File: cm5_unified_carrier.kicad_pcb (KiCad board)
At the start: 4 copper layers, 116 x 84 mm, 45 parts, among them J101 436500403, J102 484050003, J103 484050003, J104 PJ-102AH, J105 1050170001, J201 7499511002A, J401 PJ-102AH, J501 Hirose DF40C-100DS-0.4V, J601 Conn_01x02_Pin, SW501 SW_Push, U201 AG5712-LPB

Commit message: a few more minor updates
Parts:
- J201: value 7499511002A -> 7499511001A
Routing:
- net GND: vias 82 -> 81
- net /Ethernet_PoE/48V_FROM_POE: vias 29 -> 35
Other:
- board text added: "48V Input HK No PoE"
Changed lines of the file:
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@@
 			)
 		)
-		(property "Value" "7499511002A"
+		(property "Value" "7499511001A"
 			(at -5.31 23.42 0)
 			(unlocked yes)
@@
 		)
 	)
+	(gr_text "48V Input\nHK No PoE"
+		(at 120.25 62.75 0)
+		(layer "F.SilkS")
+		(effects
+			(font
+				(size 1 1)
+				(thickness 0.1)
+			)
+			(justify left bottom)
+		)
+	)
 	(gr_text "USB3 \nCamera"
 		(at 165.95 126.15 90)
@@
 	)
 	(via
-		(at 154.72 83.92)
+		(at 155.75 83.75)
 		(size 0.6)
 		(drill 0.3)
@@
 	)
 	(via
-		(at 154.58 91.07)
-		(size 0.6)
-		(drill 0.3)
-		(layers "F.Cu" "B.Cu")
-		(free yes)
-		(net 2)
-	)
-	(via
 		(at 151.26 116.64)
 		(size 0.6)
@@
 	)
 	(via
+		(at 155 87.5)
+		(size 0.6)
+		(drill 0.3)
+		(layers "F.Cu" "B.Cu")
+		(free yes)
+		(net 6)
+	)
+	(via
+		(at 154.25 84.75)
+		(size 0.6)
+		(drill 0.3)
+		(layers "F.Cu" "B.Cu")
+		(free yes)
+		(net 6)
+	)
+	(via
 		(at 156.3 96.2)
 		(size 0.6)
@@
 	)
 	(via
+		(at 153 84)
+		(size 0.6)
+		(drill 0.3)
+		(layers "F.Cu" "B.Cu")
+		(free yes)
+		(net 6)
+	)
+	(via
 		(at 137.5 92.5)
 		(size 0.6)
@@
 	)
 	(via
+		(at 154.25 86.25)
+		(size 0.6)
+		(drill 0.3)
+		(layers "F.Cu" "B.Cu")
+		(free yes)
+		(net 6)
+	)
+	(via
 		(at 154 100.2)
 		(size 0.6)
@@
 	)
 	(via
+		(at 153.25 89.75)
+		(size 0.6)
+		(drill 0.3)
+		(layers "F.Cu" "B.Cu")
+		(free yes)
+		(net 6)
+	)
+	(via
 		(at 157.2 101.5)
 		(size 0.6)
@@
 	)
 	(via
+		(at 155 89)
+		(size 0.6)
+		(drill 0.3)
+		(layers "F.Cu" "B.Cu")
+		(free yes)
+		(net 6)
+	)
+	(via
 		(at 134.7 90)
 		(size 0.6)
@@
 			)
 		)
+	)
+	(zone
+		(net 6)
+		(net_name "/Ethernet_PoE/48V_FROM_POE")
+		(layer "F.Cu")
+		(hatch edge 0.5)
+		(priority 14)
+		(connect_pads
+			(clearance 0.5)
+		)
+		(min_thickness 0.25)
+		(filled_areas_thickness no)
+		(fill yes
+			(thermal_gap 0.5)
+			(thermal_bridge_width 0.5)
+		)
+		(polygon
+			(pts
+				(xy 151.75 83.75) (xy 151.75 86.5) (xy 152.5 87.25) (xy 152.5 90.25) (xy 155.75 90.25) (xy 155.75 84.5)
+				(xy 153.75 83.75)
+			)
+		)

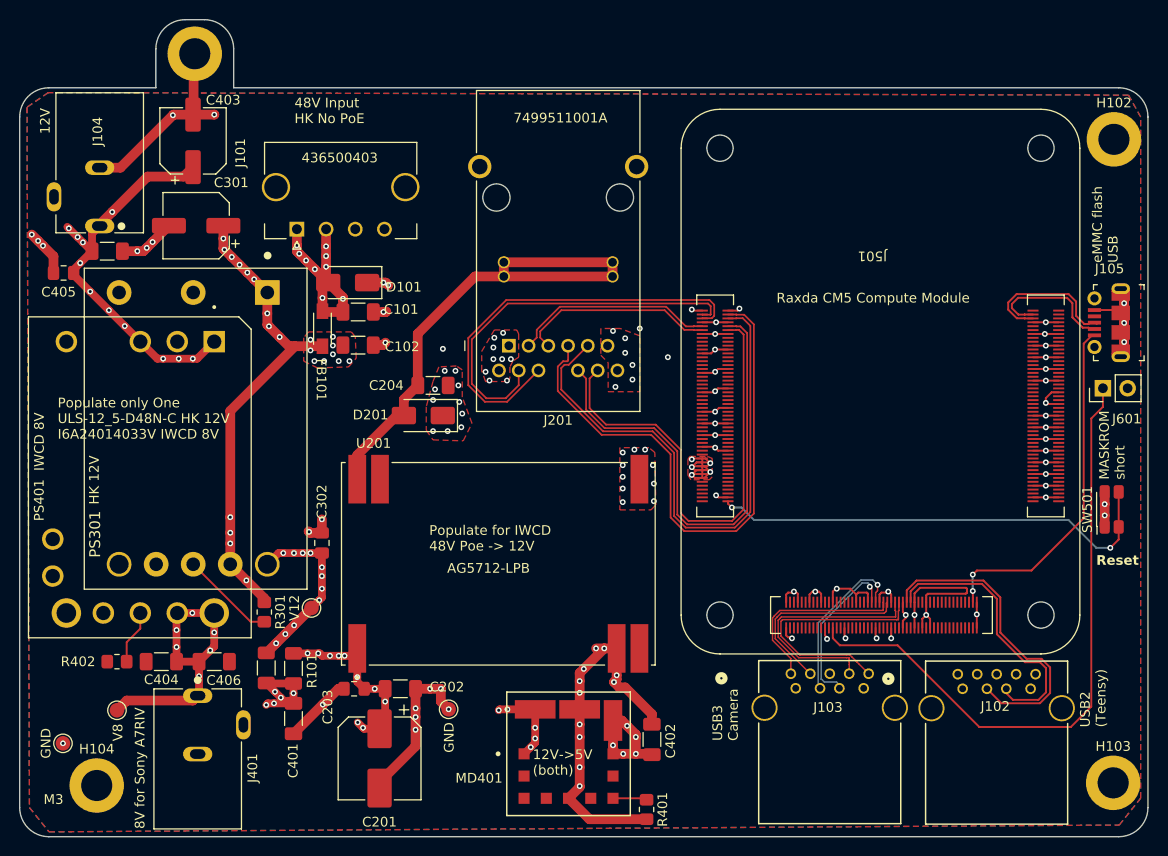
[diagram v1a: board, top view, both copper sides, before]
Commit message: Update to fix power connection mistakes in both IWCD and HK configurations. For IWCD added bridge rectifier diodes needed for PoE, for HK updated to look at correct ref voltage for the 12V generation DC/DC, rotated the TVS to correct orientation and updated input diodes to be >=100V
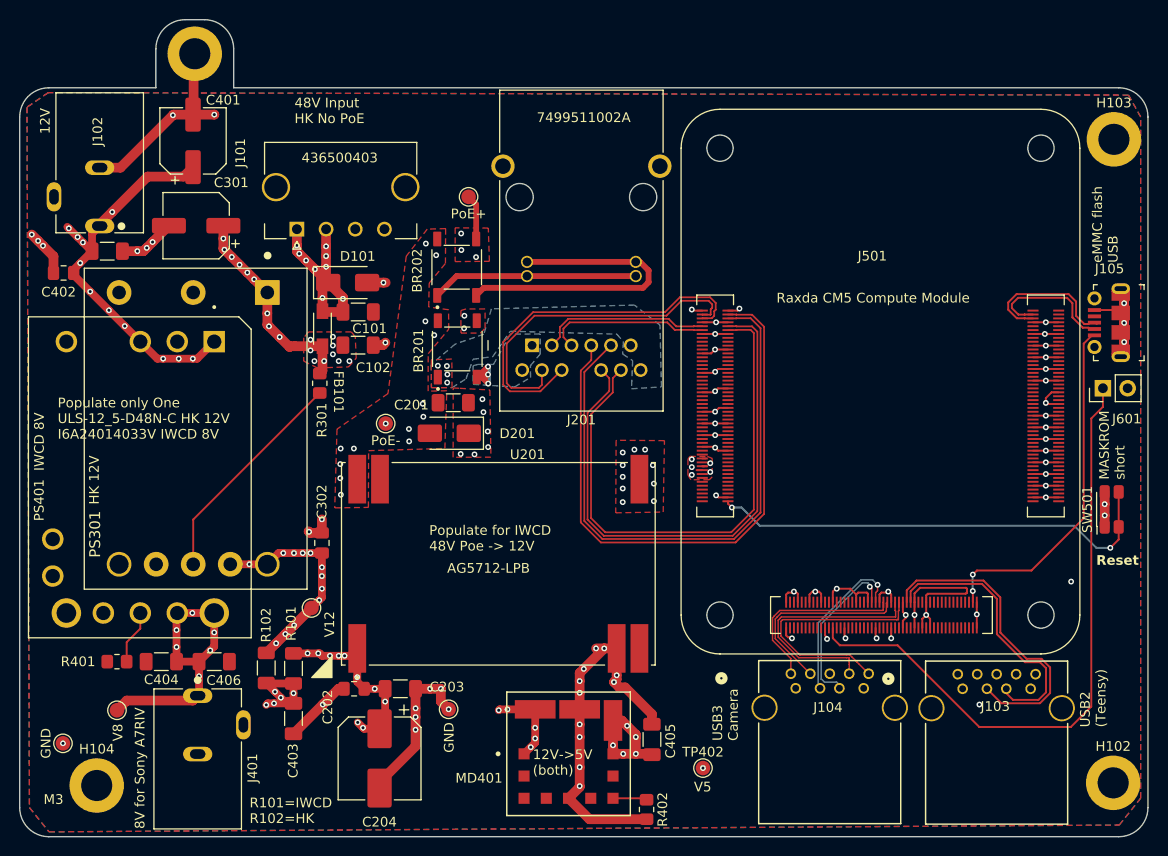
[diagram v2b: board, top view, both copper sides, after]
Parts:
- added BR201: ABS10, ABS10:SOT200P640X160-4N, F.Cu at (137.0, 85.8)
- added BR202: ABS10, ABS10:SOT200P640X160-4N, F.Cu at (136.9, 77.5)
- added TP201: PoE-, TestPoint:TestPoint_Pad_D1.5mm, F.Cu at (129.6, 93.5)
- added TP202: PoE+, TestPoint:TestPoint_Pad_D1.5mm, F.Cu at (138.2, 70.2)
- added TP402: V5, TestPoint:TestPoint_Pad_D1.5mm, F.Cu at (162.2, 128.9)
- C301: value 47uF -> 10uF
- J201: value 7499511001A -> 7499511002A
- moved R301 24.2 mm to (122.8, 89.4)
- moved D201 3.23 mm to (136.2, 94.5)
- moved C201 2.74 mm to (136.6, 91.4), turned to 0 degrees
- moved J201 2.39 mm to (144.7, 85.5)
- turned D101 to 0 degrees
- renumbered C204 to C201, C203 to C202, C202 to C203, C201 to C204, C403 to C401, C405 to C402, C401 to C403, C402 to C405, H103 to H102, H102 to H103, J104 to J102, J102 to J103, J103 to J104, R402 to R401, R401 to R402
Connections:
- C201 pad 1: /Ethernet_PoE/48V_FROM_POE -> /Ethernet_PoE/REF_FROM_POE
- C201 pad 2: Net-(D201-A2) -> /Ethernet_PoE/48V_FROM_POE
- D101 pad 1: GND -> /VIN_48
- D101 pad 2: /VIN_48 -> GND
- D201 pad 2: Net-(D201-A2) -> /Ethernet_PoE/REF_FROM_POE
- J201 pad 1: /Ethernet_PoE/48V_FROM_POE -> /Ethernet_PoE/BR201_BOT
- J201 pad 12: /Ethernet_PoE/48V_FROM_POE -> /Ethernet_PoE/BR201_TOP
- J201 pad 13: Net-(D201-A2) -> Net-(J201-V1)
- J201 pad 14: Net-(D201-A2) -> Net-(J201-V1)
- J201 pad 15: Net-(D201-A2) -> Net-(J201-V3)
- J201 pad 16: Net-(D201-A2) -> Net-(J201-V3)
- J201 pad 6: /Ethernet_PoE/48V_FROM_POE -> /Ethernet_PoE/BR201_TOP
- J201 pad 7: /Ethernet_PoE/48V_FROM_POE -> /Ethernet_PoE/BR201_BOT
- PS301 pad 7: /VIN_MURATA -> /Power_48_to_12_5/V12_FROM_48
- U201 pad 6: Net-(D201-A2) -> /Ethernet_PoE/REF_FROM_POE
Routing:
- net Net-(D201-A2): track 54.5 -> 0.00 mm
- net Net-(J201-V3): track 0.00 -> 32.4 mm
- net /VIN_MURATA: track 49.2 -> 21.6 mm, vias 22 -> 18
- net Net-(J201-V1): track 0.00 -> 21.2 mm
- net Net-(PS301-TRIM): track 9.76 -> 23.0 mm
- net +5V: track 27.7 -> 14.6 mm, vias 10 -> 11
- net /ETH_TX1-: track 50.8 -> 57.5 mm
- net /ETH_TX1+: track 49.0 -> 55.8 mm
- net /Ethernet_PoE/BR201_BOT: track 0.00 -> 6.08 mm, vias 0 -> 3
- net /ETH_TX4-: track 43.7 -> 38.3 mm
- net /ETH_TX4+: track 40.0 -> 34.6 mm
- net /Ethernet_PoE/48V_FROM_POE: track 0.00 -> 4.66 mm, vias 35 -> 21
- net /ETH_TX2-: track 57.5 -> 61.9 mm
- net /ETH_TX2+: track 58.6 -> 63.0 mm
- net /Power_48_to_12_5/V12_FROM_48: track 18.7 -> 22.5 mm, vias 11 -> 12
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- added copper zone on B.Cu, net /Ethernet_PoE/BR201_BOT
- added copper zone on B.Cu, net /Ethernet_PoE/BR201_TOP
- added copper zone on F.Cu, net /Ethernet_PoE/BR201_TOP
- added copper zone on F.Cu, net /Ethernet_PoE/REF_FROM_POE
- added copper zone on In2.Cu, net /Ethernet_PoE/REF_FROM_POE
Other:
- board text added: "R101=IWCD R102=HK"
